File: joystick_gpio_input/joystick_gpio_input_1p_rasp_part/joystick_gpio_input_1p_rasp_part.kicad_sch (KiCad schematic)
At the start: 3 parts, among them J10 Conn_01x14, J6 Conn_02x09_Odd_Even, J8 Conn_01x14

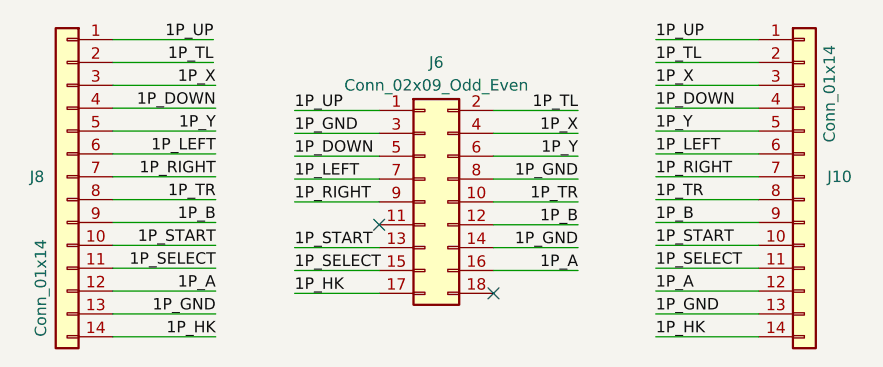
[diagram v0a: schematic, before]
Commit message: joystick gpio 스크린샷 추가
Signed-off-by: Ju, Gyeong-min <jcmh74@gmail.com>
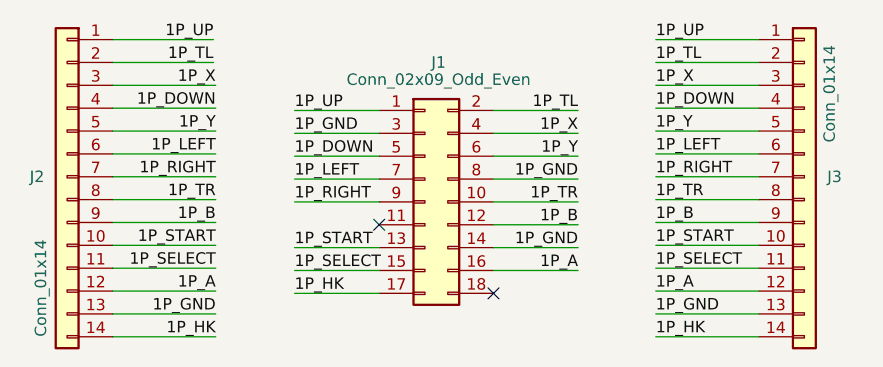
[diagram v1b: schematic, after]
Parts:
- renumbered J6 to J1, J8 to J2, J10 to J3
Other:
- title: Raspberry Pie GPIO Input Module -> Raspberry Pie GPIO Input Module (1P Part)
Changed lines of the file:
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@@
   (paper "A4")
   (title_block
-    (title "Raspberry Pie GPIO Input Module")
-    (date "2023-03-26")
+    (title "Raspberry Pie GPIO Input Module (1P Part)")
+    (date "2023-04-02")
     (rev "2")
     (company "Amos Home")
@@
   (symbol (lib_id "Connector_Generic:Conn_01x14") (at 185.42 99.695 0) (unit 1)
     (in_bom yes) (on_board yes) (dnp no)
-    (property "Reference" "J10" (at 187.96 99.695 0)
+    (property "Reference" "J3" (at 187.96 99.695 0)
       (effects (font (size 1.27 1.27)) (justify left))
     )
@@
       (project "joystick_gpio_input_1p_rasp_part"
         (path "/fa38296e-cdcc-4309-9d50-3ec5b62681ed"
-          (reference "J10") (unit 1)
+          (reference "J3") (unit 1)
         )
       )
@@
   )
   (symbol (lib_id "Connector_Generic:Conn_02x09_Odd_Even") (at 143.256 102.489 0) (unit 1)
-    (in_bom yes) (on_board yes) (dnp no) (fields_autoplaced)
-    (property "Reference" "J6" (at 144.526 86.995 0)
+    (in_bom yes) (on_board yes) (dnp no)
+    (property "Reference" "J1" (at 144.78 86.995 0)
       (effects (font (size 1.27 1.27)))
     )
-    (property "Value" "Conn_02x09_Odd_Even" (at 144.526 89.535 0)
+    (property "Value" "Conn_02x09_Odd_Even" (at 144.78 88.9 0)
       (effects (font (size 1.27 1.27)))
     )
@@
       (project "joystick_gpio_input_1p_rasp_part"
         (path "/fa38296e-cdcc-4309-9d50-3ec5b62681ed"
-          (reference "J6") (unit 1)
+          (reference "J1") (unit 1)
         )
       )
@@
   (symbol (lib_id "Connector_Generic:Conn_01x14") (at 103.505 99.695 0) (mirror y) (unit 1)
     (in_bom yes) (on_board yes) (dnp no)
-    (property "Reference" "J8" (at 100.965 99.695 0)
+    (property "Reference" "J2" (at 100.965 99.695 0)
       (effects (font (size 1.27 1.27)) (justify left))
     )
@@
       (project "joystick_gpio_input_1p_rasp_part"
         (path "/fa38296e-cdcc-4309-9d50-3ec5b62681ed"
-          (reference "J8") (unit 1)
+          (reference "J2") (unit 1)
         )
       )
